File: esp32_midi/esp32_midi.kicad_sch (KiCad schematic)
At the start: 18 parts, among them J2 5V-12V, J3 USB_C_Receptacle_USB2.0, SW1 SW_SPST, U1 ESP32-S3-WROOM-2, U2 AMS1117-5.0, U3 AMS1117-3.3

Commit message: Add ordentliche-teile
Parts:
- J3: footprint Diode_SMD:D_SOD-123 -> usb_c:USB-C-SMD_MC-311D
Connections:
- net analogorgie/OUTPUT0 is gone; now on net 64buttons/OUTPUT1: U1.20 (GPIO12/TOUCH12/ADC2_CH1/FSPICLK/FSPIIO6/SUBSPICLK)
- net 64buttons/OUTPUT0: now also U1.19 (GPIO11/TOUCH11/ADC2_CH0/FSPID/FSPIIO5/SUBSPID); no longer U1.18 (GPIO10/TOUCH10/ADC1_CH9/FSPICS0/FSPIIO4/SUBSPICS0)
- net 64buttons/OUTPUT1: no longer U1.19 (GPIO11/TOUCH11/ADC2_CH0/FSPID/FSPIIO5/SUBSPID)
- net lichtorgie/DATA: now also U1.9 (GPIO16/U0CTS/ADC2_CH5/XTAL_32K_NH5)
- net analogorgie/OUTPUT1: no longer names the net of U1.21 (GPIO13/TOUCH13/ADC2_CH2/FSPIQ/FSPIIO7/SUBSPIQ)
- new net analogorgie/OUTPUT: U1.18 (GPIO10/TOUCH10/ADC1_CH9/FSPICS0/FSPIIO4/SUBSPICS0)
- no-connect marks 2 -> 4
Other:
- sheet analogorgie ports: added OUTPUT, SEL4; removed OUTPUT0, OUTPUT1
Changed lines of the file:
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@@
   (junction (at 81.28 44.45) (diameter 0) (color 0 0 0 0)
   )
+  (junction (at 73.66 76.2) (diameter 0) (color 0 0 0 0)
+  )
   (junction (at 72.39 73.66) (diameter 0) (color 0 0 0 0)
   )
@@
   )
   (no_connect (at 267.97 106.68))
+  (no_connect (at 267.97 127))
   (no_connect (at 267.97 104.14))
+  (no_connect (at 267.97 129.54))
   (wire (pts (xy 214.63 44.45) (xy 226.06 44.45))
     (stroke (width 0) (type default))
   )
+  (wire (pts (xy 59.69 102.87) (xy 74.93 102.87))
+    (stroke (width 0) (type default))
+  )
   (wire (pts (xy 59.69 97.79) (xy 72.39 97.79))
     (stroke (width 0) (type default))
@@
     (stroke (width 0) (type default))
   )
-  (wire (pts (xy 74.93 86.36) (xy 78.74 86.36))
-    (stroke (width 0) (type default))
-  )
   (wire (pts (xy 243.84 44.45) (xy 247.65 44.45))
     (stroke (width 0) (type default))
@@
     (stroke (width 0) (type default))
   )
+  (wire (pts (xy 80.01 80.01) (xy 80.01 81.28))
+    (stroke (width 0) (type default))
+  )
   (wire (pts (xy 63.5 144.78) (xy 67.31 144.78))
     (stroke (width 0) (type default))
   )
+  (wire (pts (xy 64.77 78.74) (xy 78.74 78.74))
+    (stroke (width 0) (type default))
+  )
   (wire (pts (xy 250.19 74.93) (xy 254 74.93))
     (stroke (width 0) (type default))
   )
-  (wire (pts (xy 78.74 82.55) (xy 78.74 86.36))
-    (stroke (width 0) (type default))
-  )
-  (wire (pts (xy 73.66 83.82) (xy 77.47 83.82))
+  (wire (pts (xy 76.2 147.32) (xy 76.2 90.17))
     (stroke (width 0) (type default))
   )
@@
     (stroke (width 0) (type default))
   )
-  (wire (pts (xy 74.93 78.74) (xy 74.93 74.93))
-    (stroke (width 0) (type default))
-  )
   (wire (pts (xy 71.12 71.12) (xy 71.12 67.31))
     (stroke (width 0) (type default))
@@
     (stroke (width 0) (type default))
   )
+  (wire (pts (xy 81.28 74.93) (xy 74.93 74.93))
+    (stroke (width 0) (type default))
+  )
   (wire (pts (xy 265.43 44.45) (xy 267.97 44.45))
     (stroke (width 0) (type default))
   )
-  (wire (pts (xy 76.2 77.47) (xy 81.28 77.47))
+  (wire (pts (xy 76.2 90.17) (xy 81.28 90.17))
     (stroke (width 0) (type default))
   )
@@
     (stroke (width 0) (type default))
   )
+  (wire (pts (xy 78.74 77.47) (xy 81.28 77.47))
+    (stroke (width 0) (type default))
+  )
   (wire (pts (xy 68.58 90.17) (xy 68.58 66.04))
     (stroke (width 0) (type default))
   )
-  (wire (pts (xy 78.74 82.55) (xy 81.28 82.55))
-    (stroke (width 0) (type default))
-  )
-  (wire (pts (xy 73.66 100.33) (xy 73.66 83.82))
+  (wire (pts (xy 74.93 74.93) (xy 74.93 102.87))
     (stroke (width 0) (type default))
   )
@@
     (stroke (width 0) (type default))
   )
-  (wire (pts (xy 76.2 81.28) (xy 64.77 81.28))
-    (stroke (width 0) (type default))
-  )
   (wire (pts (xy 39.37 27.94) (xy 39.37 26.67))
     (stroke (width 0) (type default))
@@
     (stroke (width 0) (type default))
   )
-  (wire (pts (xy 59.69 100.33) (xy 73.66 100.33))
-    (stroke (width 0) (type default))
-  )
   (wire (pts (xy 267.97 44.45) (xy 279.4 44.45))
     (stroke (width 0) (type default))
   )
+  (wire (pts (xy 63.5 147.32) (xy 76.2 147.32))
+    (stroke (width 0) (type default))
+  )
   (wire (pts (xy 77.47 92.71) (xy 77.47 120.65))
     (stroke (width 0) (type default))
@@
     (stroke (width 0) (type default))
   )
-  (wire (pts (xy 74.93 74.93) (xy 81.28 74.93))
-    (stroke (width 0) (type default))
-  )
   (wire (pts (xy 64.77 68.58) (xy 69.85 68.58))
     (stroke (width 0) (type default))
@@
     (stroke (width 0) (type default))
   )
-  (wire (pts (xy 76.2 77.47) (xy 76.2 81.28))
-    (stroke (width 0) (type default))
-  )
-  (wire (pts (xy 64.77 78.74) (xy 74.93 78.74))
-    (stroke (width 0) (type default))
-  )
-  (wire (pts (xy 74.93 102.87) (xy 74.93 86.36))
-    (stroke (width 0) (type default))
-  )
   (wire (pts (xy 77.47 92.71) (xy 81.28 92.71))
     (stroke (width 0) (type default))
@@
     (stroke (width 0) (type default))
   )
-  (wire (pts (xy 59.69 102.87) (xy 74.93 102.87))
-    (stroke (width 0) (type default))
-  )
   (wire (pts (xy 72.39 73.66) (xy 72.39 97.79))
     (stroke (width 0) (type default))
@@
     (stroke (width 0) (type default))
   )
+  (wire (pts (xy 73.66 100.33) (xy 59.69 100.33))
+    (stroke (width 0) (type default))
+  )
+  (wire (pts (xy 78.74 78.74) (xy 78.74 77.47))
+    (stroke (width 0) (type default))
+  )
   (wire (pts (xy 59.69 95.25) (xy 71.12 95.25))
     (stroke (width 0) (type default))
@@
     (stroke (width 0) (type default))
   )
-  (wire (pts (xy 77.47 80.01) (xy 77.47 83.82))
-    (stroke (width 0) (type default))
-  )
   (wire (pts (xy 69.85 64.77) (xy 81.28 64.77))
     (stroke (width 0) (type default))
   )
+  (wire (pts (xy 64.77 81.28) (xy 80.01 81.28))
+    (stroke (width 0) (type default))
+  )
   (wire (pts (xy 71.12 95.25) (xy 71.12 71.12))
     (stroke (width 0) (type default))
@@
     (stroke (width 0) (type default))
   )
+  (wire (pts (xy 81.28 80.01) (xy 80.01 80.01))
+    (stroke (width 0) (type default))
+  )
   (wire (pts (xy 67.31 115.57) (xy 69.85 115.57))
     (stroke (width 0) (type default))
@@
     (stroke (width 0) (type default))
   )
+  (wire (pts (xy 73.66 76.2) (xy 73.66 100.33))
+    (stroke (width 0) (type default))
+  )
   (wire (pts (xy 224.79 74.93) (xy 228.6 74.93))
-    (stroke (width 0) (type default))
-  )
-  (wire (pts (xy 77.47 80.01) (xy 81.28 80.01))
     (stroke (width 0) (type default))
   )
@@
       (effects (font (size 1.27 1.27)))
     )
-    (property "Footprint" "Diode_SMD:D_SOD-123" (at 256.54 114.3 0)
+    (property "Footprint" "usb_c:USB-C-SMD_MC-311D" (at 256.54 114.3 0)
       (effects (font (size 1.27 1.27)) hide)
     )
@@
       (effects (font (size 1.27 1.27)) (justify right))
     )
-    (pin "OUTPUT0" input (at 59.69 100.33 0)
-      (effects (font (size 1.27 1.27)) (justify right))
-    )
-    (pin "OUTPUT1" input (at 59.69 102.87 0)
-      (effects (font (size 1.27 1.27)) (justify right))
-    )
+    (pin "SEL4" input (at 59.69 100.33 0)
+      (effects (font (size 1.27 1.27)) (justify right))
+    )
+    (pin "OUTPUT" input (at 59.69 102.87 0)
+      (effects (font (size 1.27 1.27)) (justify right))
+    )

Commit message: Started work on PCB
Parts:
- removed C4, C5: 100n, Capacitor_SMD:C_0402_1005Metric, symbol Device:C
- removed J3: USB_C_Receptacle_USB2.0, usb_c:USB-C-SMD_MC-311D, symbol Connector:USB_C_Receptacle_USB2.0
- removed U2: AMS1117-5.0, Package_TO_SOT_SMD:SOT-223-3_TabPin2, symbol Regulator_Linear:AMS1117-5.0
- added R7, R8: 5k1, Resistor_SMD:R_0402_1005Metric, symbol Device:R
- added USBC1: MC-311D, usb_c:USB-C-SMD_MC-311D, symbol usb_c_bobby:MC-311D
- SW1: footprint (none) -> Button_Switch_THT:SW_PUSH_6mm_H13mm
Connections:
- net 5V_USB: now also USBC1.A4-B9 (VBUS), USBC1.B4-A9 (VBUS)
- net GND: now also R7.2, R8.1, USBC1.1 (SHIELD), USBC1.2 (SHIELD), USBC1.3 (SHIELD), USBC1.4 (SHIELD), USBC1.A1-B12 (GND), USBC1.B1-A12 (GND)
- net USB2.0_D+: now also USBC1.A6 (DP1), USBC1.B6 (DP2)
- net USB2.0_D-: now also USBC1.A7 (DN1), USBC1.B7 (DN2)
- net flasher/ESP_EN: no longer U1.27 (GPIO0/BOOT)
- net dcdc_lm2596/OUT: now reaches D2.2 (A)
- net buttonsorgie/OUTPUT2: now reaches U1.21 (GPIO13/TOUCH13/ADC2_CH2/FSPIQ/FSPIIO7/SUBSPIQ)
- net buttonsorgie/SEL0 renamed analogorgie/SEL0
- net buttonsorgie/SEL1 renamed analogorgie/SEL1
- net buttonsorgie/SEL2 renamed analogorgie/SEL2
- net buttonsorgie/SEL3 renamed analogorgie/SEL3
- net buttonsorgie/SEL4 renamed analogorgie/SEL4
- new net: R7.1, USBC1.A5 (CC1)
- new net: R8.2, USBC1.B5 (CC2)
- new net flasher/ESP_IO0: U1.27 (GPIO0/BOOT)
- no-connect marks 4 -> 2
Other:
- sheet 64buttons renamed buttonsorgie
- added sheet dcdc_lm2596 (dcdc_lm2596.kicad_sch)
- sheet buttonsorgie: file 64buttons.kicad_sch -> buttonsorgie.kicad_sch
- sheet buttonsorgie ports: added OUTPUT2; removed none
- moved on the sheet: D1, J2

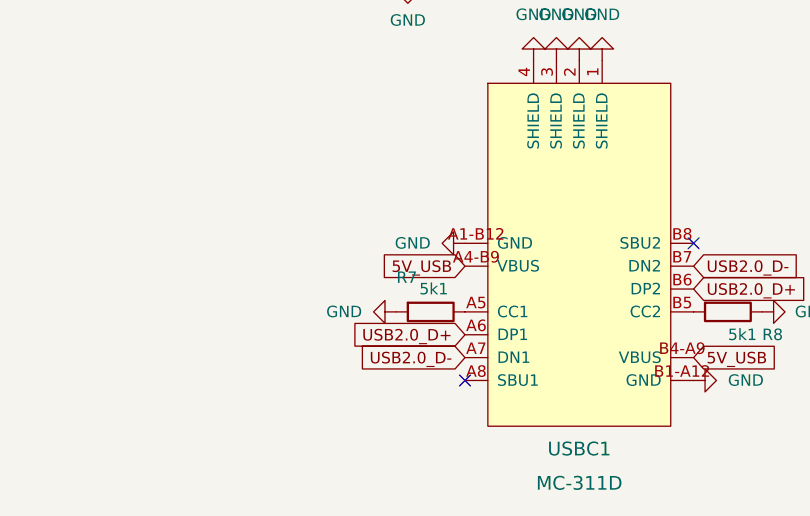
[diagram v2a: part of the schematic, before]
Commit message: More PCB implementations
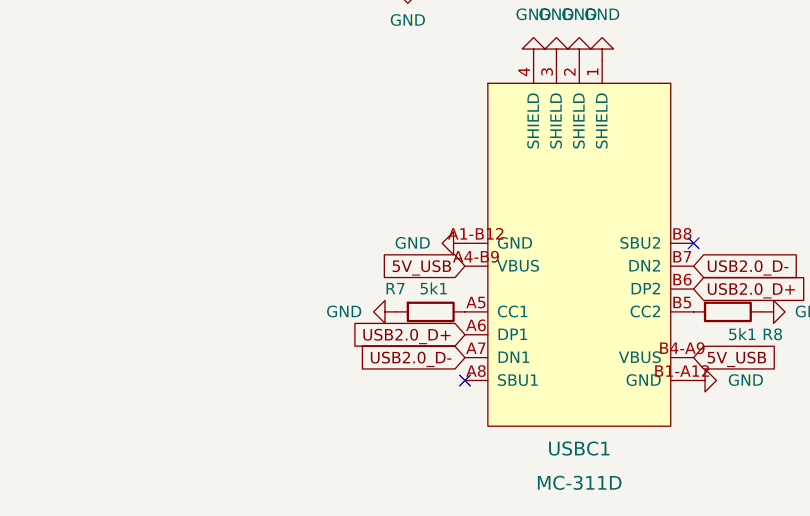
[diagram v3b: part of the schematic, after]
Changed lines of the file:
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@@
   (symbol (lib_id "Device:R") (at 199.39 140.97 270) (unit 1)
     (in_bom yes) (on_board yes) (dnp no)
-    (property "Reference" "R7" (at 195.58 137.16 90)
+    (property "Reference" "R7" (at 194.31 138.43 90)
       (effects (font (size 1.27 1.27)) (justify left))
     )

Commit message: More pcb
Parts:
- added H1, H2, H3, H4: MountingHole_Pad, MountingHole:MountingHole_4mm_Pad_Via, symbol Mechanical:MountingHole_Pad
- C1, C3, C6, C?: footprint Capacitor_SMD:C_0402_1005Metric -> Capacitor_SMD:C_1206_3216Metric
- R1, R7, R8: footprint Resistor_SMD:R_0402_1005Metric -> Resistor_SMD:R_1206_3216Metric
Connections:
- net GND: now also H1.1, H2.1, H3.1, H4.1

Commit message: Net improvements
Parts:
- added NT102: NetTie_3, NetTie:NetTie-3_SMD_Pad0.5mm, symbol Device:NetTie_3
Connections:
- net 5V_USB: now also NT102.2; no longer USBC1.A4-B9 (VBUS), USBC1.B4-A9 (VBUS)
- new net THIN_5V_USB0: NT102.1, USBC1.A4-B9 (VBUS)
- new net THIN_5V_USB1: NT102.3, USBC1.B4-A9 (VBUS)
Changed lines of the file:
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@@
+    (stroke (width 0) (type default))
+  )
+  (wire (pts (xy 256.54 44.45) (xy 257.81 44.45))
     (stroke (width 0) (type default))
   )
@@
     (stroke (width 0) (type default))
   )
-  (wire (pts (xy 256.54 44.45) (xy 257.81 44.45))
-    (stroke (width 0) (type default))
-  )
   (wire (pts (xy 33.02 55.88) (xy 34.29 55.88))
     (stroke (width 0) (type default))
@@
     (stroke (width 0) (type default))
   )
+  (global_label "THIN_5V_USB1" (shape input) (at 191.77 160.02 180) (fields_autoplaced)
+    (effects (font (size 1.27 1.27)) (justify right))
+    (property "Intersheetrefs" "${INTERSHEET_REFS}" (at 175.378 160.02 0)
+      (effects (font (size 1.27 1.27)) (justify right) hide)
+    )
+  )
   (global_label "USB2.0_D-" (shape input) (at 203.2 146.05 180) (fields_autoplaced)
     (effects (font (size 1.27 1.27)) (justify right))
@@
     )
   )
-  (global_label "5V_USB" (shape input) (at 228.6 146.05 0) (fields_autoplaced)
-    (effects (font (size 1.27 1.27)) (justify left))
-    (property "Intersheetrefs" "${INTERSHEET_REFS}" (at 238.5815 146.05 0)
+  (global_label "5V_USB" (shape input) (at 196.85 157.48 0) (fields_autoplaced)
+    (effects (font (size 1.27 1.27)) (justify left))
+    (property "Intersheetrefs" "${INTERSHEET_REFS}" (at 206.8315 157.48 0)
       (effects (font (size 1.27 1.27)) (justify left) hide)
     )
@@
     )
   )
+  (global_label "THIN_5V_USB0" (shape input) (at 203.2 135.89 180) (fields_autoplaced)
+    (effects (font (size 1.27 1.27)) (justify right))
+    (property "Intersheetrefs" "${INTERSHEET_REFS}" (at 186.808 135.89 0)
+      (effects (font (size 1.27 1.27)) (justify right) hide)
+    )
+  )
   (global_label "5V_USB2" (shape input) (at 33.02 45.72 0) (fields_autoplaced)
     (effects (font (size 1.27 1.27)) (justify left))
@@
     )
   )
+  (global_label "THIN_5V_USB1" (shape input) (at 228.6 146.05 0) (fields_autoplaced)
+    (effects (font (size 1.27 1.27)) (justify left))
+    (property "Intersheetrefs" "${INTERSHEET_REFS}" (at 244.992 146.05 0)
+      (effects (font (size 1.27 1.27)) (justify left) hide)
+    )
+  )
   (global_label "DISPLAY_MOSI" (shape input) (at 114.3 27.94 180) (fields_autoplaced)
     (effects (font (size 1.27 1.27)) (justify right))
@@
     )
   )
+  (global_label "THIN_5V_USB0" (shape input) (at 191.77 157.48 180) (fields_autoplaced)
+    (effects (font (size 1.27 1.27)) (justify right))
+    (property "Intersheetrefs" "${INTERSHEET_REFS}" (at 175.378 157.48 0)
+      (effects (font (size 1.27 1.27)) (justify right) hide)
+    )
+  )
   (global_label "DISPLAY_DC" (shape input) (at 114.3 33.02 180) (fields_autoplaced)
     (effects (font (size 1.27 1.27)) (justify right))
@@
     )
     (property "Referenzen zwischen Schaltplänen" "${INTERSHEET_REFS}" (at 100.9087 32.9406 0)
-      (effects (font (size 1.27 1.27)) (justify right) hide)
-    )
-  )
-  (global_label "5V_USB" (shape input) (at 203.2 135.89 180) (fields_autoplaced)
-    (effects (font (size 1.27 1.27)) (justify right))
-    (property "Intersheetrefs" "${INTERSHEET_REFS}" (at 193.2185 135.89 0)
       (effects (font (size 1.27 1.27)) (justify right) hide)
     )
@@
         )
       )
+    )
+  )
+  (symbol (lib_id "Device:NetTie_3") (at 194.31 157.48 0) (unit 1)
+    (in_bom no) (on_board yes) (dnp no)
+    (property "Reference" "NT102" (at 194.31 152.4 0)
+      (effects (font (size 1.27 1.27)) hide)
+    )
+    (property "Value" "NetTie_3" (at 194.31 154.94 0)
+      (effects (font (size 1.27 1.27)))
+    )
+    (property "Footprint" "NetTie:NetTie-3_SMD_Pad0.5mm" (at 194.31 157.48 0)
+      (effects (font (size 1.27 1.27)) hide)
+    )
+    (property "Datasheet" "~" (at 194.31 157.48 0)
+      (effects (font (size 1.27 1.27)) hide)
+    )
+    (pin "1")
+    (pin "2")
+    (pin "3")
+    (instances
+      (project "esp32_midi"
+        (path "/e33c0603-5c0d-4712-ab63-5756d1504b4c"
+          (reference "NT102") (unit 1)
+        )
+      )

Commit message: Everything changed
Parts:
- D1: value D -> 1N4148
- D2, D3, D4: value D -> SS54; footprint Diode_SMD:D_SOD-123 -> Diode_SMD:D_SMA
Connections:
- net +12V: now also J2.1; no longer J2.2
- net GND: now also J2.2; no longer J2.1

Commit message: First load of bug fixes
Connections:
- no-connect marks 2 -> 13
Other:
- sheet buttonsorgie ports: added +3.3V; removed none
- sheet flasher ports: added +3.3V; removed none
- moved on the sheet: J2
